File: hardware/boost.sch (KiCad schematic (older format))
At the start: 7 parts, among them U6 MT3608

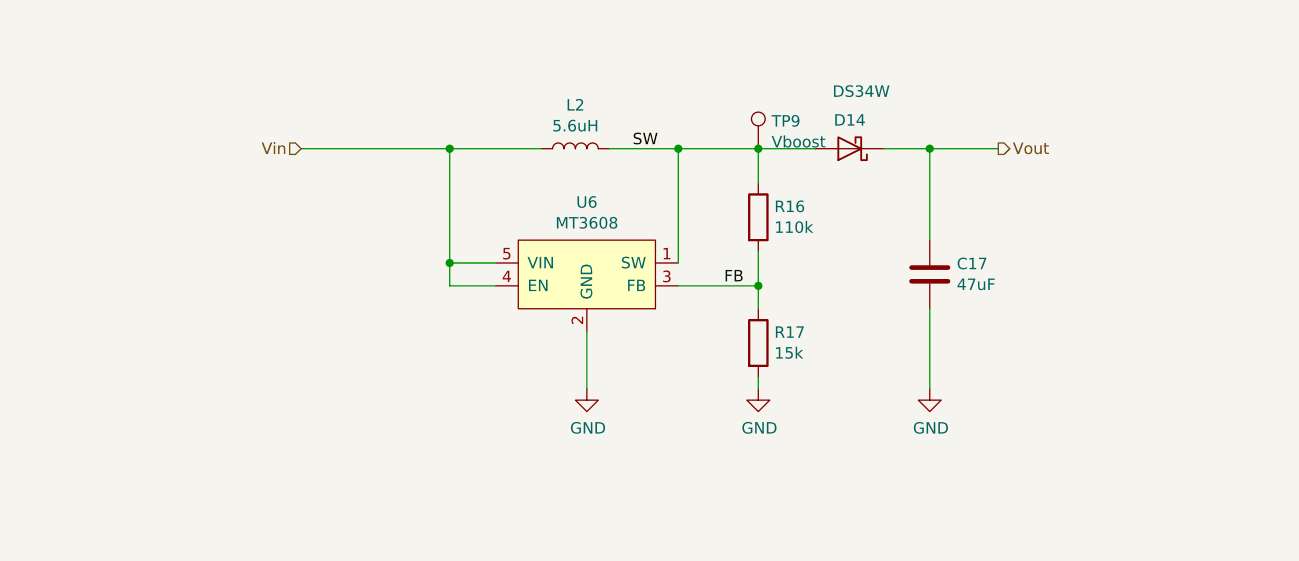
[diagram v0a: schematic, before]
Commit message: Changed to pure-serial topology. Changed to beefier mcu.
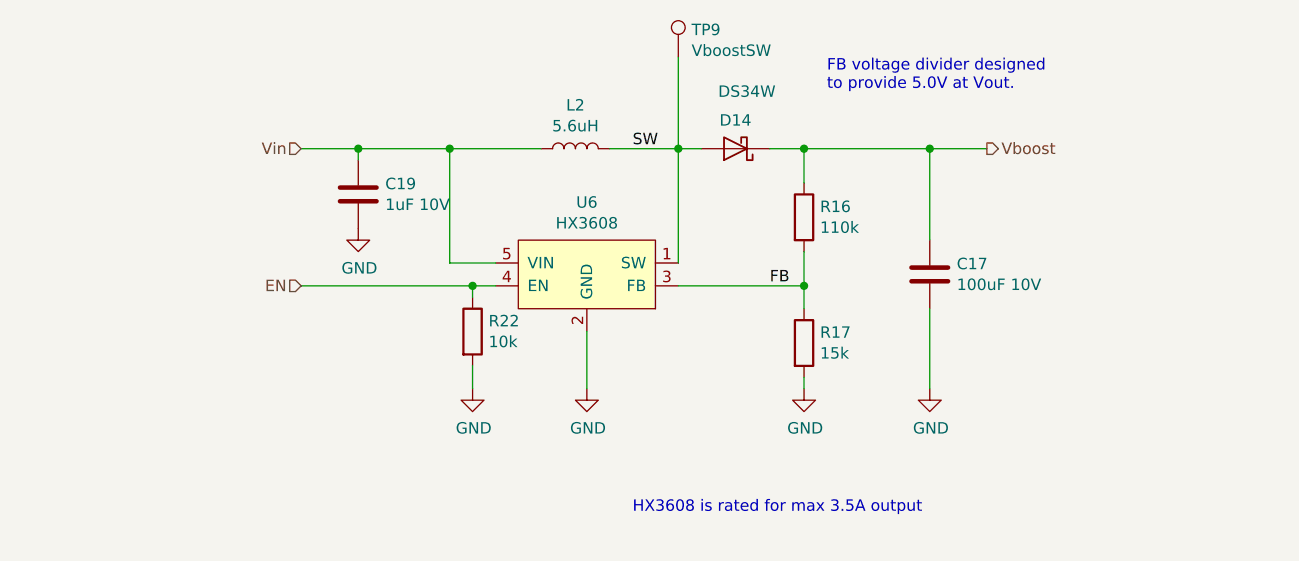
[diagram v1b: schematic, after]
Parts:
- added C19: 1uF 10V, symbol Device:C
- added R22: 10k, Resistor_SMD:R_0603_1608Metric_Pad1.05x0.95mm_HandSolder, symbol Device:R
- C17: value 47uF -> 100uF 10V; footprint Capacitor_SMD:C_0805_2012Metric_Pad1.15x1.40mm_HandSolder -> Capacitor_SMD:C_1210_3225Metric_Pad1.42x2.65mm_HandSolder
- L2: footprint Inductor_SMD:L_4.5x4.8_H3_Handsolder -> Inductor_SMD:L_Taiyo-Yuden_NR-40xx_HandSoldering
- TP9: value Vboost -> VboostSW
- U6: value MT3608 -> HX3608
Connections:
- net GND: now also C19.2, R22.2
- net SW: no longer R16.1
- net Vin: now also C19.1; no longer U6.4 (EN)
- net Vout renamed Vboost
- net Vboost: now also R16.1
- new net EN: R22.1, U6.4 (EN)
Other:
- note added: "FB voltage divider designed\nto provide 5.0V at Vout."
- note added: "HX3608 is rated for max 3.5A output"
- moved on the sheet: D14, R16, R17, TP9
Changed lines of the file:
@@
-EESchema Schematic File Version 4
+EESchema Schematic File Version 5
 LIBS:pi-supercap-ups-cache
-EELAYER 26 0
+EELAYER 30 0
 EELAYER END
 $Descr A4 11693 8268
 encoding utf-8
-Sheet 7 8
+Sheet 4 8
 Title ""
 Date ""
@@
 AR Path="/5CA73F16/5CA6B4E8" Ref="C17"  Part="1"
 F 0 "C17" H 5018 2296 50  0000 L CNN
-F 1 "47uF" H 5018 2205 50  0000 L CNN
-F 2 "Capacitor_SMD:C_0805_2012Metric_Pad1.15x1.40mm_HandSolder" H 4938 2100 50  0001 C CNN
+F 1 "100uF 10V" H 5018 2205 50  0000 L CNN
+F 2 "Capacitor_SMD:C_1210_3225Metric_Pad1.42x2.65mm_HandSolder" H 4938 2100 50  0001 C CNN
 F 3 "~" H 4900 2250 50  0001 C CNN
 	1    4900 2250
@@
 AR Path="/5CA73F16/5CA6B4F5" Ref="U6"  Part="1"
 F 0 "U6" H 3400 2565 50  0000 C CNN
-F 1 "MT3608" H 3400 2474 50  0000 C CNN
+F 1 "HX3608" H 3400 2474 50  0000 C CNN
 F 2 "Package_TO_SOT_SMD:SOT-23-6_Handsoldering" H 3400 2450 50  0001 C CNN
 F 3 "" H 3400 2450 50  0001 C CNN
@@
 F 0 "L2" V 3540 1700 50  0000 C CNN
 F 1 "5.6uH" V 3449 1700 50  0000 C CNN
-F 2 "Inductor_SMD:L_4.5x4.8_H3_Handsolder" H 3350 1700 50  0001 C CNN
+F 2 "Inductor_SMD:L_Taiyo-Yuden_NR-40xx_HandSoldering" H 3350 1700 50  0001 C CNN
 F 3 "~" H 3350 1700 50  0001 C CNN
 	1    3350 1700
@@
 	2800 1700 3200 1700
 Wire Wire Line
-	3000 2300 2800 2300
-Wire Wire Line
-	2800 2300 2800 2200
-Connection ~ 2800 2200
-Wire Wire Line
 	3800 2200 3800 1700
 Wire Wire Line
@@
 L Diode:1N5820 D?
 U 1 1 5CA6B513
-P 4550 1700
+P 4050 1700
 AR Path="/5C3480BB/5CA6B513" Ref="D?"  Part="1"
 AR Path="/5C3476D8/5CA6B513" Ref="D?"  Part="1"
 AR Path="/5CA73F16/5CA6B513" Ref="D14"  Part="1"
-F 0 "D14" H 4550 1576 50  0000 C CNN
-F 1 "DS34W" H 4500 1450 50  0000 C CNN
-F 2 "Diode_SMD:D_SOD-123F" H 4550 1525 50  0001 C CNN
-F 3 "http://www.vishay.com/docs/88526/1n5820.pdf" H 4550 1700 50  0001 C CNN
-	1    4550 1700
+F 0 "D14" H 4050 1576 50  0000 C CNN
+F 1 "DS34W" H 4000 1450 50  0000 C CNN
+F 2 "Diode_SMD:D_SOD-123F" H 4050 1525 50  0001 C CNN
+F 3 "http://www.vishay.com/docs/88526/1n5820.pdf" H 4050 1700 50  0001 C CNN
+	1    4050 1700
 	-1   0    0    1
 $EndComp
-Connection ~ 3800 1700
 $Comp
 L Device:R R?
 U 1 1 5CA6B51B
-P 4150 2000
+P 4350 2000
 AR Path="/5CA6B51B" Ref="R?"  Part="1"
 AR Path="/5C3480BB/5CA6B51B" Ref="R?"  Part="1"
 AR Path="/5CA73F16/5CA6B51B" Ref="R16"  Part="1"
-F 0 "R16" H 4220 2046 50  0000 L CNN
-F 1 "110k" H 4220 1955 50  0000 L CNN
-F 2 "Resistor_SMD:R_0603_1608Metric_Pad1.05x0.95mm_HandSolder" V 4080 2000 50  0001 C CNN
-F 3 "~" H 4150 2000 50  0001 C CNN
-	1    4150 2000
+F 0 "R16" H 4420 2046 50  0000 L CNN
+F 1 "110k" H 4420 1955 50  0000 L CNN
+F 2 "Resistor_SMD:R_0603_1608Metric_Pad1.05x0.95mm_HandSolder" V 4280 2000 50  0001 C CNN
+F 3 "~" H 4350 2000 50  0001 C CNN
+	1    4350 2000
 	1    0    0    -1
 $EndComp
@@
 L Device:R R?
 U 1 1 5CA6B522
-P 4150 2550
+P 4350 2550
 AR Path="/5CA6B522" Ref="R?"  Part="1"
 AR Path="/5C3480BB/5CA6B522" Ref="R?"  Part="1"
 AR Path="/5CA73F16/5CA6B522" Ref="R17"  Part="1"
-F 0 "R17" H 4220 2596 50  0000 L CNN
-F 1 "15k" H 4220 2505 50  0000 L CNN
-F 2 "Resistor_SMD:R_0603_1608Metric_Pad1.05x0.95mm_HandSolder" V 4080 2550 50  0001 C CNN
-F 3 "~" H 4150 2550 50  0001 C CNN
-	1    4150 2550
+F 0 "R17" H 4420 2596 50  0000 L CNN
+F 1 "15k" H 4420 2505 50  0000 L CNN
+F 2 "Resistor_SMD:R_0603_1608Metric_Pad1.05x0.95mm_HandSolder" V 4280 2550 50  0001 C CNN
+F 3 "~" H 4350 2550 50  0001 C CNN
+	1    4350 2550
 	1    0    0    -1
 $EndComp
@@
 L power:GND #PWR?
 U 1 1 5CA6B529
-P 4150 2750
+P 4350 2750
 AR Path="/5CA6B529" Ref="#PWR?"  Part="1"
 AR Path="/5C3480BB/5CA6B529" Ref="#PWR?"  Part="1"
 AR Path="/5CA73F16/5CA6B529" Ref="#PWR045"  Part="1"
-F 0 "#PWR045" H 4150 2500 50  0001 C CNN
-F 1 "GND" H 4155 2577 50  0000 C CNN
-F 2 "" H 4150 2750 50  0001 C CNN
-F 3 "" H 4150 2750 50  0001 C CNN
-	1    4150 2750
-	1    0    0    -1
-$EndComp
-Wire Wire Line
-	3800 2300 4150 2300
-Wire Wire Line
-	4150 2300 4150 2150
-Wire Wire Line
-	4150 2300 4150 2400
-Connection ~ 4150 2300
-Wire Wire Line
-	4150 1850 4150 1700
-Wire Wire Line
-	4150 2750 4150 2700
+F 0 "#PWR045" H 4350 2500 50  0001 C CNN
+F 1 "GND" H 4355 2577 50  0000 C CNN
+F 2 "" H 4350 2750 50  0001 C CNN
+F 3 "" H 4350 2750 50  0001 C CNN
+	1    4350 2750
+	1    0    0    -1
+$EndComp
+Wire Wire Line
+	4350 2300 4350 2150
+Wire Wire Line
+	4350 2300 4350 2400
+Connection ~ 4350 2300
+Wire Wire Line
+	4350 2750 4350 2700
 Wire Wire Line
 	4900 2750 4900 2400
 Wire Wire Line
 	4900 2100 4900 1700
-Connection ~ 4150 1700
-Wire Wire Line
-	2150 1700 2800 1700
-Wire Wire Line
-	4150 1700 4400 1700
+Wire Wire Line
+	2150 1700 2400 1700
 Text Label 3600 1700 0    50   ~ 0
 SW
-Text Label 4000 2300 0    50   ~ 0
+Text Label 4200 2300 0    50   ~ 0
 FB
 Connection ~ 4900 1700
 Wire Wire Line
-	4900 1700 5200 1700
+	4900 1700 5150 1700
 Text HLabel 2150 1700 0    50   Input ~ 0
 Vin
-Text HLabel 5200 1700 2    50   Output ~ 0
-Vout
-Wire Wire Line
-	4700 1700 4900 1700
-Wire Wire Line
-	3800 1700 4150 1700
 $Comp
 L Connector:TestPoint TP?
 U 1 1 5CAAC10F
-P 4150 1700
+P 3800 1300
 AR Path="/5C345D5A/5CAAC10F" Ref="TP?"  Part="1"
 AR Path="/5CA73F16/5CAAC10F" Ref="TP9"  Part="1"
-F 0 "TP9" H 4208 1820 50  0000 L CNN
-F 1 "Vboost" H 4208 1729 50  0000 L CNN
-F 2 "TestPoint:TestPoint_Keystone_5000-5004_Miniature" H 4350 1700 50  0001 C CNN
-F 3 "~" H 4350 1700 50  0001 C CNN
-	1    4150 1700
-	1    0    0    -1
-$EndComp
+F 0 "TP9" H 3858 1420 50  0000 L CNN
+F 1 "VboostSW" H 3858 1329 50  0000 L CNN
+F 2 "TestPoint:TestPoint_Keystone_5000-5004_Miniature" H 4000 1300 50  0001 C CNN
+F 3 "~" H 4000 1300 50  0001 C CNN
+	1    3800 1300
+	1    0    0    -1
+$EndComp
+Wire Wire Line
+	3900 1700 3800 1700
+Connection ~ 3800 1700
+Wire Wire Line
+	4350 1850 4350 1700
+Wire Wire Line
+	4350 1700 4200 1700
+Connection ~ 4350 1700
+Wire Wire Line
+	3800 1300 3800 1700
+Wire Wire Line
+	3800 2300 4350 2300
+Text Notes 4450 1450 0    50   ~ 0
+FB voltage divider designed\nto provide 5.0V at Vout.
+Text HLabel 5150 1700 2    50   Output ~ 0
+Vboost
+Wire Wire Line
+	4350 1700 4900 1700
+$Comp
+L Device:C C?
+U 1 1 5CF608F8
+P 2400 1900
+AR Path="/5CF608F8" Ref="C?"  Part="1"
+AR Path="/5C3480BB/5CF608F8" Ref="C?"  Part="1"
+AR Path="/5CA73F16/5CF608F8" Ref="C19"  Part="1"
+F 0 "C19" H 2518 1946 50  0000 L CNN
+F 1 "1uF 10V" H 2518 1855 50  0000 L CNN
+F 2 "" H 2438 1750 50  0001 C CNN
+F 3 "~" H 2400 1900 50  0001 C CNN
+	1    2400 1900
+	1    0    0    -1
+$EndComp
+Wire Wire Line
+	2400 1750 2400 1700
+Connection ~ 2400 1700
+Wire Wire Line
+	2400 1700 2800 1700
+$Comp
+L power:GND #PWR?
+U 1 1 5CF60DAB
+P 2400 2050
+AR Path="/5CF60DAB" Ref="#PWR?"  Part="1"
+AR Path="/5C3480BB/5CF60DAB" Ref="#PWR?"  Part="1"
+AR Path="/5CA73F16/5CF60DAB" Ref="#PWR0104"  Part="1"
+F 0 "#PWR0104" H 2400 1800 50  0001 C CNN
+F 1 "GND" H 2405 1877 50  0000 C CNN
+F 2 "" H 2400 2050 50  0001 C CNN
+F 3 "" H 2400 2050 50  0001 C CNN
+	1    2400 2050
+	1    0    0    -1
+$EndComp
+Text Notes 3600 3300 0    50   ~ 0
+HX3608 is rated for max 3.5A output
+$Comp
+L Device:R R?
+U 1 1 5D545585
+P 2900 2500
+AR Path="/5D545585" Ref="R?"  Part="1"
+AR Path="/5C3480BB/5D545585" Ref="R?"  Part="1"
+AR Path="/5CA73F16/5D545585" Ref="R22"  Part="1"
+F 0 "R22" H 2970 2546 50  0000 L CNN
+F 1 "10k" H 2970 2455 50  0000 L CNN
+F 2 "Resistor_SMD:R_0603_1608Metric_Pad1.05x0.95mm_HandSolder" V 2830 2500 50  0001 C CNN
+F 3 "~" H 2900 2500 50  0001 C CNN
+	1    2900 2500
+	1    0    0    -1
+$EndComp
+Text HLabel 2150 2300 0    50   Input ~ 0
+EN
+Wire Wire Line
+	2150 2300 2900 2300
+$Comp
+L power:GND #PWR?
+U 1 1 5D5460DA
+P 2900 2750
+AR Path="/5D5460DA" Ref="#PWR?"  Part="1"
+AR Path="/5C3480BB/5D5460DA" Ref="#PWR?"  Part="1"
+AR Path="/5CA73F16/5D5460DA" Ref="#PWR0107"  Part="1"
+F 0 "#PWR0107" H 2900 2500 50  0001 C CNN
+F 1 "GND" H 2905 2577 50  0000 C CNN
+F 2 "" H 2900 2750 50  0001 C CNN
+F 3 "" H 2900 2750 50  0001 C CNN
+	1    2900 2750
+	1    0    0    -1
+$EndComp
+Wire Wire Line
+	2900 2350 2900 2300
+Connection ~ 2900 2300
+Wire Wire Line
+	2900 2300 3000 2300
+Wire Wire Line
+	2900 2750 2900 2650
 $EndSCHEMATC

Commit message: Layout partially done before change of plans
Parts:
- removed D14: DS34W, Diode_SMD:D_SOD-123F, symbol Diode:1N5820
- removed U6: HX3608, Package_TO_SOT_SMD:SOT-23-6_Handsoldering, symbol pi-supercap-ups:MT3608
- added R2: 10k, Resistor_SMD:R_0603_1608Metric_Pad1.05x0.95mm_HandSolder, symbol Device:R
- added SW1: SW_SPST, Connector_PinHeader_2.54mm:PinHeader_1x02_P2.54mm_Vertical, symbol Switch:SW_SPST
- added U4: TPS61022, custom:TPS61022RWUR, symbol pi-supercap-ups:TPS61022
- C19: footprint (none) -> Capacitor_SMD:C_0603_1608Metric_Pad1.05x0.95mm_HandSolder
- L2: value 5.6uH -> 1uH; footprint Inductor_SMD:L_Taiyo-Yuden_NR-40xx_HandSoldering -> Inductor_SMD:L_Wuerth_HCI-1350; Notes (none) -> BCIHP0750-1R0
- R16: value 110k -> 147k
- R17: value 15k -> 20k
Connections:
- net EN: now also R2.1; no longer R22.1
- net FB: now also U4.4 (FB)
- net GND: now also SW1.1 (A), U4.1 (GND)
- net SW: now also U4.2 (SW)
- net Vboost: now also U4.3 (VOUT)
- net Vin: now also U4.7 (VIN)
- new net: R22.1, U4.6 (MODE)
- new net: R2.2, SW1.2 (B), U4.5 (EN)
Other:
- note removed: "HX3608 is rated for max 3.5A output"
- moved on the sheet: C17, R16, R17, R22

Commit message: revE ready for production
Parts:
- removed R22: 10k, Resistor_SMD:R_0603_1608Metric_Pad1.05x0.95mm_HandSolder, symbol Device:R
- removed TP9: VboostSW, TestPoint:TestPoint_Keystone_5000-5004_Miniature, symbol Connector:TestPoint
- added C6: 47uF 10V, Capacitor_SMD:C_1206_3216Metric_Pad1.42x1.75mm_HandSolder, symbol Device:C
- C17: value 100uF 10V -> 47uF 10V; footprint Capacitor_SMD:C_1210_3225Metric_Pad1.42x2.65mm_HandSolder -> Capacitor_SMD:C_1206_3216Metric_Pad1.42x1.75mm_HandSolder
- C19: value 1uF 10V -> 10uF 10V
- L2: footprint Inductor_SMD:L_Wuerth_HCI-1350 -> Inductor_SMD:L_Abracon_ASPI-0630LR; Notes BCIHP0750-1R0 -> Shun Xiang Nuo Elec SMMS0630-1R0M
- renumbered U4 to U2
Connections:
- net GND: now also U2.6 (MODE), C6.2
- net Vboost: now also C6.1
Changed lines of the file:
@@
 $Descr A4 11693 8268
 encoding utf-8
-Sheet 3 6
+Sheet 3 7
 Title ""
 Date ""
@@
 AR Path="/5CA73F16/5CA6B4E8" Ref="C17"  Part="1"
 F 0 "C17" H 4968 2496 50  0000 L CNN
-F 1 "100uF 10V" H 4968 2405 50  0000 L CNN
-F 2 "Capacitor_SMD:C_1210_3225Metric_Pad1.42x2.65mm_HandSolder" H 4888 2300 50  0001 C CNN
+F 1 "47uF 10V" H 4968 2405 50  0000 L CNN
+F 2 "Capacitor_SMD:C_1206_3216Metric_Pad1.42x1.75mm_HandSolder" H 4888 2300 50  0001 C CNN
 F 3 "~" H 4850 2450 50  0001 C CNN
 	1    4850 2450
@@
 F 0 "L2" V 3540 1700 50  0000 C CNN
 F 1 "1uH" V 3449 1700 50  0000 C CNN
-F 2 "Inductor_SMD:L_Wuerth_HCI-1350" H 3350 1700 50  0001 C CNN
+F 2 "Inductor_SMD:L_Abracon_ASPI-0630LR" H 3350 1700 50  0001 C CNN
 F 3 "" H 3350 1700 50  0001 C CNN
-F 4 "BCIHP0750-1R0" V 3350 1700 50  0001 C CNN "Notes"
+F 4 "Shun Xiang Nuo Elec SMMS0630-1R0M" V 3350 1700 50  0001 C CNN "Notes"
 	1    3350 1700
 	0    -1   -1   0
@@
 Text HLabel 2150 1700 0    50   Input ~ 0
 Vin
-$Comp
-L Connector:TestPoint TP?
-U 1 1 5CAAC10F
-P 3800 1300
-AR Path="/5C345D5A/5CAAC10F" Ref="TP?"  Part="1"
-AR Path="/5CA73F16/5CAAC10F" Ref="TP9"  Part="1"
-F 0 "TP9" H 3858 1420 50  0000 L CNN
-F 1 "VboostSW" H 3858 1329 50  0000 L CNN
-F 2 "TestPoint:TestPoint_Keystone_5000-5004_Miniature" H 4000 1300 50  0001 C CNN
-F 3 "~" H 4000 1300 50  0001 C CNN
-	1    3800 1300
-	1    0    0    -1
-$EndComp
-Connection ~ 3800 1700
-Wire Wire Line
-	3800 1300 3800 1700
 Wire Wire Line
 	3800 2600 4350 2600
@@
 AR Path="/5CA73F16/5CF608F8" Ref="C19"  Part="1"
 F 0 "C19" H 2518 1946 50  0000 L CNN
-F 1 "1uF 10V" H 2518 1855 50  0000 L CNN
+F 1 "10uF 10V" H 2518 1855 50  0000 L CNN
 F 2 "Capacitor_SMD:C_0603_1608Metric_Pad1.05x0.95mm_HandSolder" H 2438 1750 50  0001 C CNN
 F 3 "~" H 2400 1900 50  0001 C CNN
@@
 	1    0    0    -1
 $EndComp
-$Comp
-L Device:R R?
-U 1 1 5D545585
-P 2800 2900
-AR Path="/5D545585" Ref="R?"  Part="1"
-AR Path="/5C3480BB/5D545585" Ref="R?"  Part="1"
-AR Path="/5CA73F16/5D545585" Ref="R22"  Part="1"
-F 0 "R22" H 2870 2946 50  0000 L CNN
-F 1 "10k" H 2870 2855 50  0000 L CNN
-F 2 "Resistor_SMD:R_0603_1608Metric_Pad1.05x0.95mm_HandSolder" V 2730 2900 50  0001 C CNN
-F 3 "~" H 2800 2900 50  0001 C CNN
-	1    2800 2900
-	1    0    0    -1
-$EndComp
 Text HLabel 1500 2600 0    50   Input ~ 0
 EN
@@
 $EndComp
 $Comp
-L pi-supercap-ups:TPS61022 U4
+L pi-supercap-ups:TPS61022 U2
 U 1 1 5D5AC086
 P 3400 2400
-F 0 "U4" H 3400 2865 50  0000 C CNN
+F 0 "U2" H 3400 2865 50  0000 C CNN
 F 1 "TPS61022" H 3400 2774 50  0000 C CNN
 F 2 "custom:TPS61022RWUR" H 3450 2600 50  0001 C CNN
@@
 	3800 2300 4350 2300
 Wire Wire Line
-	5500 2300 4850 2300
+	5500 2300 5450 2300
 Connection ~ 4350 2300
 Connection ~ 4850 2300
@@
 Wire Wire Line
 	2800 2500 3000 2500
-Wire Wire Line
-	2800 2750 2800 2500
 $Comp
 L Switch:SW_SPST SW1
@@
 Wire Wire Line
 	2150 3200 2150 3150
+$Comp
+L Device:C C?
+U 1 1 5D8155D9
+P 5450 2450
+AR Path="/5D8155D9" Ref="C?"  Part="1"
+AR Path="/5C3480BB/5D8155D9" Ref="C?"  Part="1"
+AR Path="/5CA73F16/5D8155D9" Ref="C6"  Part="1"
+F 0 "C6" H 5568 2496 50  0000 L CNN
+F 1 "47uF 10V" H 5568 2405 50  0000 L CNN
+F 2 "Capacitor_SMD:C_1206_3216Metric_Pad1.42x1.75mm_HandSolder" H 5488 2300 50  0001 C CNN
+F 3 "~" H 5450 2450 50  0001 C CNN
+	1    5450 2450
+	1    0    0    -1
+$EndComp
+Connection ~ 5450 2300
+Wire Wire Line
+	5450 2300 4850 2300
+$Comp
+L power:GND #PWR?
+U 1 1 5D815A89
+P 5450 2700
+AR Path="/5D815A89" Ref="#PWR?"  Part="1"
+AR Path="/5C3480BB/5D815A89" Ref="#PWR?"  Part="1"
+AR Path="/5CA73F16/5D815A89" Ref="#PWR024"  Part="1"
+F 0 "#PWR024" H 5450 2450 50  0001 C CNN
+F 1 "GND" H 5455 2527 50  0000 C CNN
+F 2 "" H 5450 2700 50  0001 C CNN
+F 3 "" H 5450 2700 50  0001 C CNN
+	1    5450 2700
+	1    0    0    -1
+$EndComp
+Wire Wire Line
+	5450 2600 5450 2700
+Wire Wire Line
+	2800 3050 2800 2500
 $EndSCHEMATC

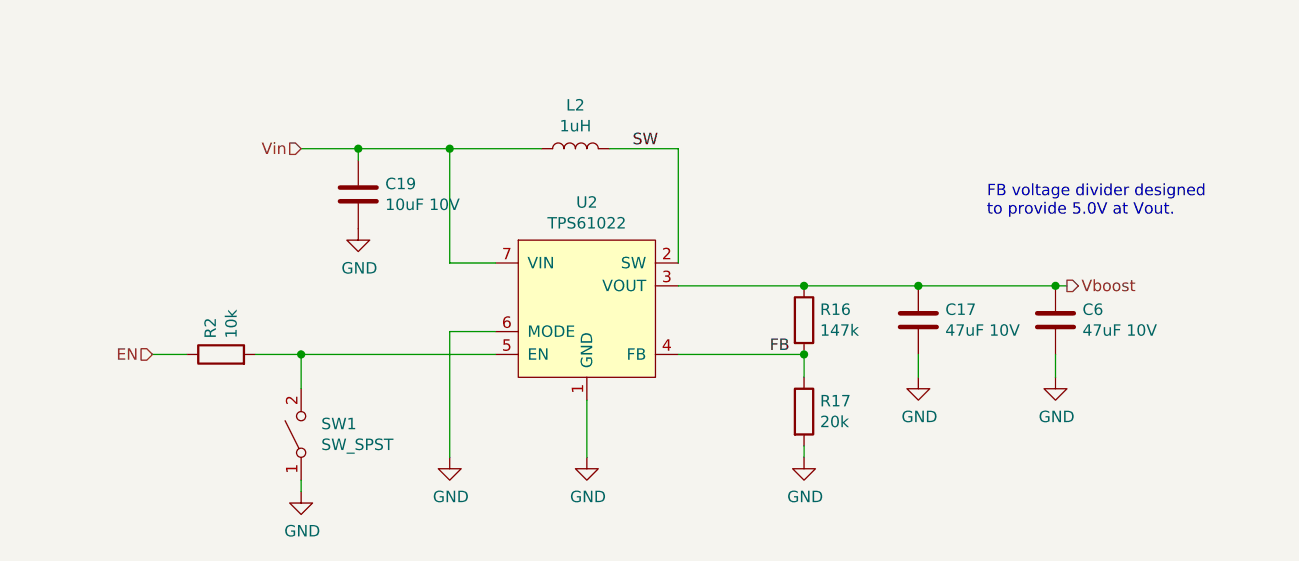
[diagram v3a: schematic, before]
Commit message: Fixed wrong footprints & passive component values.
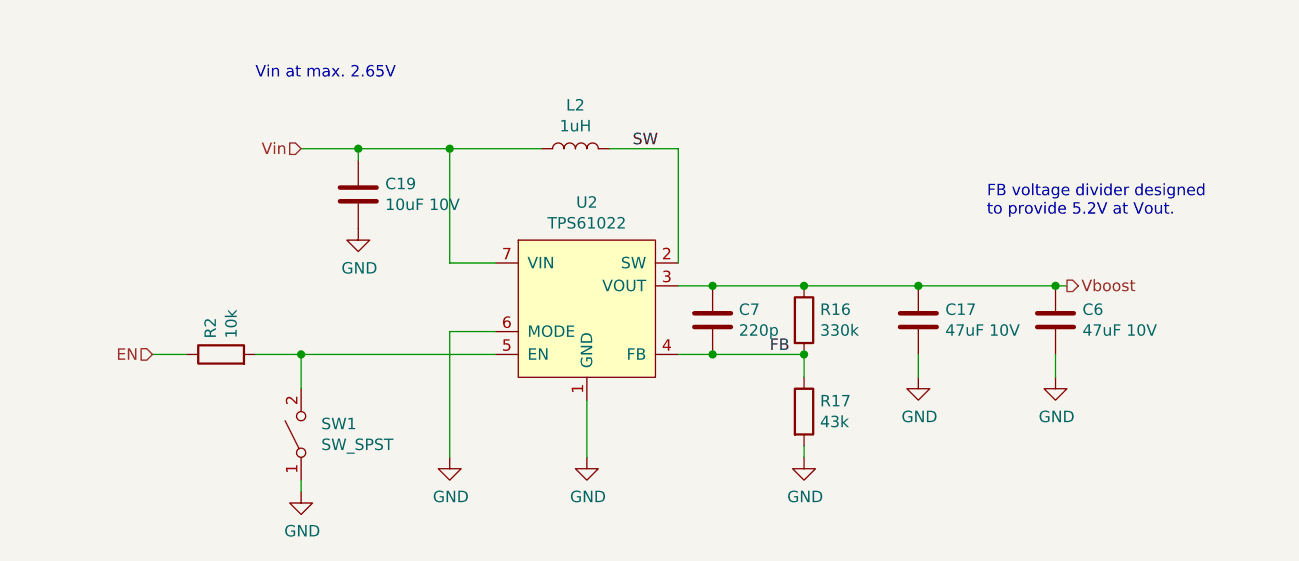
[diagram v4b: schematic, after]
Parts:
- added C7: 220p, Capacitor_SMD:C_0603_1608Metric_Pad1.05x0.95mm_HandSolder, symbol Device:C
- R16: value 147k -> 330k
- R17: value 20k -> 43k
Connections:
- net FB: now also C7.2
- net Vboost: now also C7.1
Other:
- note added: "FB voltage divider designed\nto provide 5.2V at Vout."
- note added: "Vin at max. 2.65V"
- note removed: "FB voltage divider designed\nto provide 5.0V at Vout."
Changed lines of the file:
@@
 AR Path="/5CA73F16/5CA6B51B" Ref="R16"  Part="1"
 F 0 "R16" H 4420 2496 50  0000 L CNN
-F 1 "147k" H 4420 2405 50  0000 L CNN
+F 1 "330k" H 4420 2405 50  0000 L CNN
 F 2 "Resistor_SMD:R_0603_1608Metric_Pad1.05x0.95mm_HandSolder" V 4280 2450 50  0001 C CNN
 F 3 "~" H 4350 2450 50  0001 C CNN
@@
 AR Path="/5CA73F16/5CA6B522" Ref="R17"  Part="1"
 F 0 "R17" H 4420 2896 50  0000 L CNN
-F 1 "20k" H 4420 2805 50  0000 L CNN
+F 1 "43k" H 4420 2805 50  0000 L CNN
 F 2 "Resistor_SMD:R_0603_1608Metric_Pad1.05x0.95mm_HandSolder" V 4280 2850 50  0001 C CNN
 F 3 "~" H 4350 2850 50  0001 C CNN
@@
 Vin
 Wire Wire Line
-	3800 2600 4350 2600
+	3800 2600 3950 2600
 Text Notes 5150 2000 0    50   ~ 0
-FB voltage divider designed\nto provide 5.0V at Vout.
+FB voltage divider designed\nto provide 5.2V at Vout.
 Text HLabel 5500 2300 2    50   Output ~ 0
 Vboost
@@
 	3400 3050 3400 2800
 Wire Wire Line
-	3800 2300 4350 2300
+	3800 2300 3950 2300
 Wire Wire Line
 	5500 2300 5450 2300
@@
 Wire Wire Line
 	2800 3050 2800 2500
+Text Notes 1950 1400 0    50   ~ 0
+Vin at max. 2.65V
+Connection ~ 3950 2300
+Wire Wire Line
+	3950 2300 4350 2300
+Connection ~ 3950 2600
+Wire Wire Line
+	3950 2600 4350 2600
+$Comp
+L Device:C C7
+U 1 1 5D913E0F
+P 3950 2450
+F 0 "C7" H 4065 2496 50  0000 L CNN
+F 1 "220p" H 4065 2405 50  0000 L CNN
+F 2 "Capacitor_SMD:C_0603_1608Metric_Pad1.05x0.95mm_HandSolder" H 3988 2300 50  0001 C CNN
+F 3 "~" H 3950 2450 50  0001 C CNN
+	1    3950 2450
+	1    0    0    -1
+$EndComp
 $EndSCHEMATC
